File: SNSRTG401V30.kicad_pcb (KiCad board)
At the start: 2 copper layers, 44 x 44 mm, 83 parts, among them J1 Conn_01x04, J10 Conn_01x02, J2 USB_C_Receptacle_USB2.0_16P, J3 Conn_01x06, J4 Conn_01x04, J5 Conn_01x06, J6 Conn_01x04, J7 Conn_01x04, J8 Conn_01x04, J9 JDY-25M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

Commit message: new Gerber generaated
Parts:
- moved C22 0.25 mm to (93.1, 34.6)
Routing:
- net TRG01: track 52.1 -> 96.4 mm, vias 4 -> 3
- net +3.3V: track 307.8 -> 280.4 mm, vias 3 -> 2
- net GND: track 351.3 -> 371.1 mm, vias 1 -> 2
- net SPI1-MISO: track 51.5 -> 70.7 mm, vias 3 -> 1
- net SPI1-SCK: track 72.1 -> 55.7 mm, vias 2 -> 3
- net IM-L/R: track 15.9 -> 30.8 mm
- net TXD2: track 50.7 -> 37.0 mm
- net Net-(J8-Pin_1): track 8.05 -> 20.4 mm, vias 1 -> 0
- net I2C1-SCL: track 80.0 -> 89.9 mm
- net 5VENBL: track 33.3 -> 25.3 mm
- net IM-DATA: track 25.1 -> 31.3 mm
- net I2C1-SDA: track 82.3 -> 88.3 mm
- net 5VINP: track 37.2 -> 31.8 mm, vias 0 -> 2
- net SWCLK: track 24.7 -> 19.4 mm
- net SPI1-MOSI: track 91.9 -> 86.7 mm
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
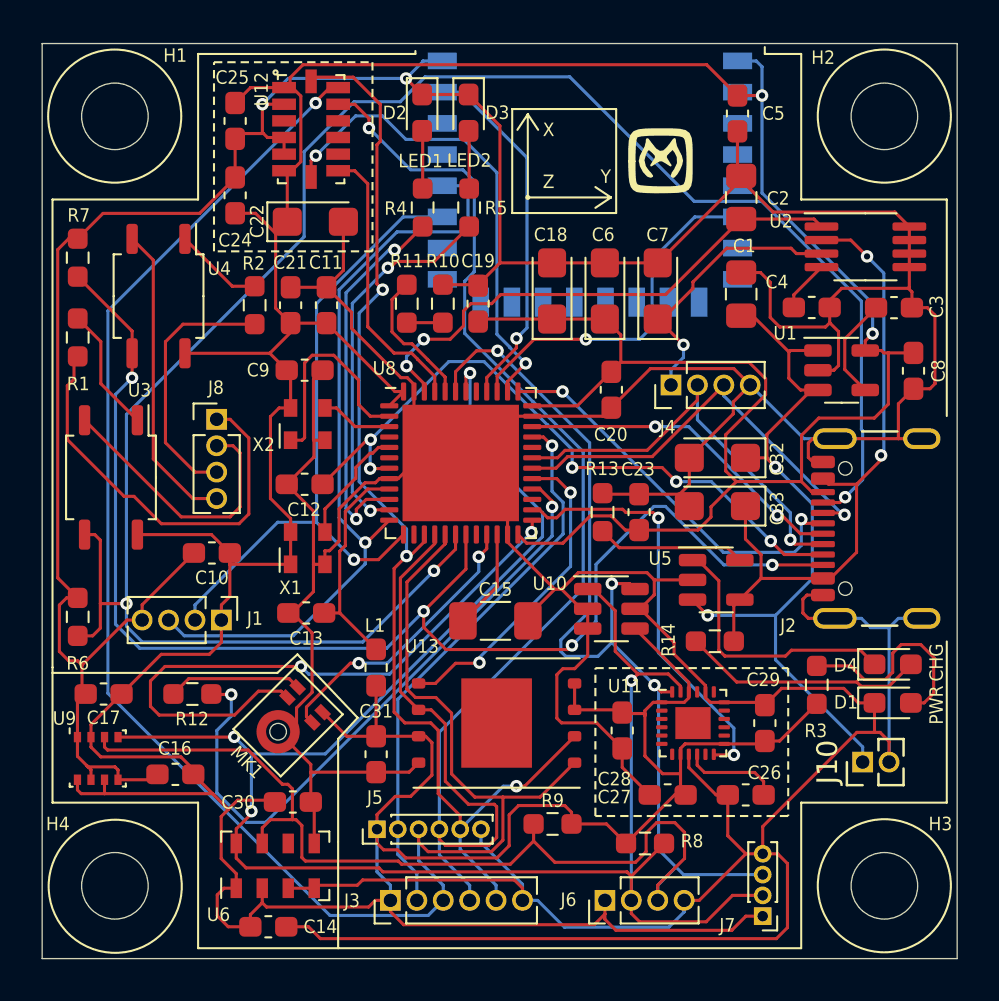
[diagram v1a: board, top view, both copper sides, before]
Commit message: DFM Issue of Lion Circuits Resolved.
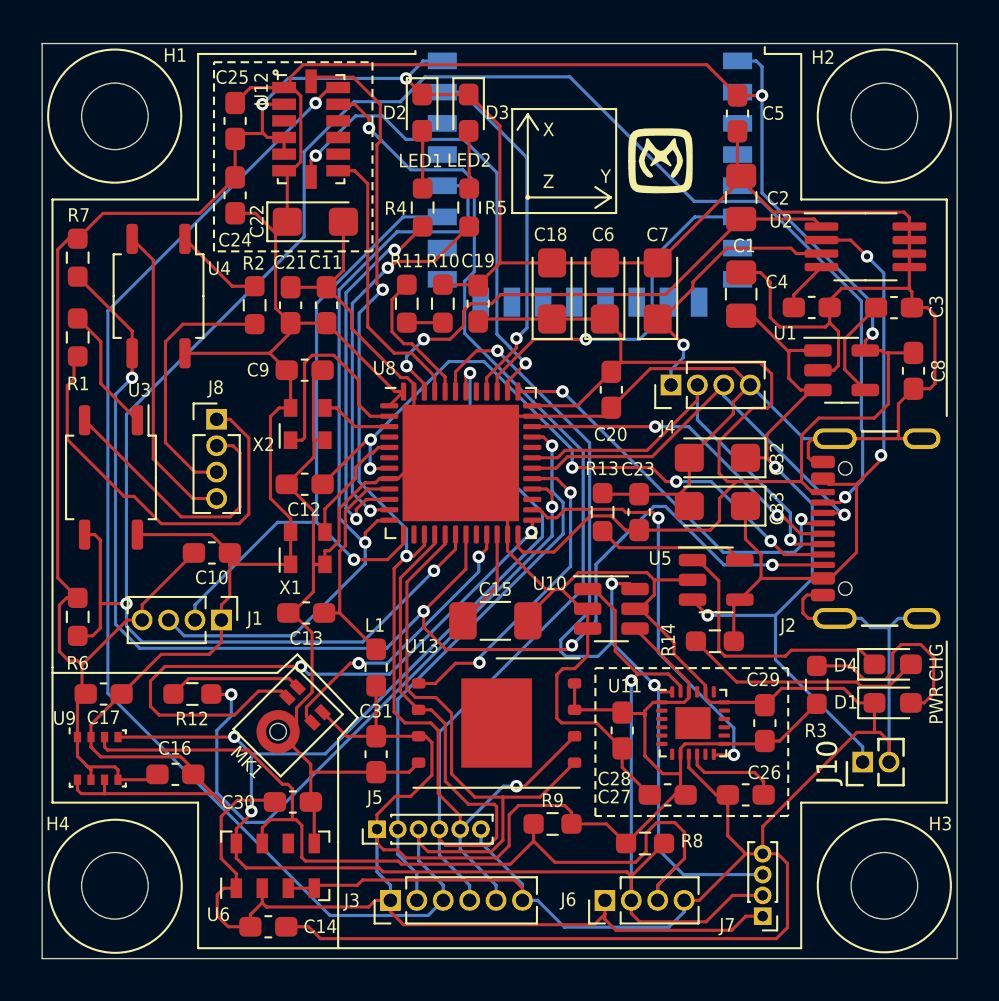
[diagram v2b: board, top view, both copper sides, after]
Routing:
- net +3.3V: track 280.4 -> 282.9 mm
- net GND: track 371.1 -> 371.6 mm
